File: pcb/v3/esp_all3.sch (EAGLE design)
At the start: 23 parts

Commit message: updated schematic
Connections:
- net N$25 renamed 3V3
- net N$26 renamed DHT_SIG
- net N$28 renamed TTL_DIMM
- removed net N$23: ESP.D5
- removed net N$29: ESP.D1, PIR.OUT
- new net N$16: ESP.D1
- new net PIR: ESP.D5, PIR.OUT
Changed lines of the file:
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@@
 </segment>
 </net>
-<net name="N$23" class="0">
+<net name="PIR" class="0">
 <segment>
 <pinref part="ESP" gate="G$1" pin="D5"/>
-<wire x1="93.98" y1="45.72" x2="99.06" y2="45.72" width="0.1524" layer="91"/>
-</segment>
-</net>
-<net name="N$26" class="0">
+<wire x1="93.98" y1="45.72" x2="111.76" y2="45.72" width="0.1524" layer="91"/>
+<wire x1="111.76" y1="45.72" x2="111.76" y2="83.82" width="0.1524" layer="91"/>
+<pinref part="PIR" gate="G$1" pin="OUT"/>
+<wire x1="111.76" y1="83.82" x2="-5.08" y2="83.82" width="0.1524" layer="91"/>
+<wire x1="-5.08" y1="83.82" x2="-5.08" y2="88.9" width="0.1524" layer="91"/>
+</segment>
+</net>
+<net name="DHT_SIG" class="0">
 <segment>
 <pinref part="ESP" gate="G$1" pin="D4"/>
@@
 </segment>
 </net>
-<net name="N$28" class="0">
+<net name="TTL_DIMM" class="0">
 <segment>
 <pinref part="ESP" gate="G$1" pin="D2"/>
@@
 <pinref part="DIMMING" gate="G$1" pin="G"/>
 <wire x1="132.08" y1="88.9" x2="104.14" y2="88.9" width="0.1524" layer="91"/>
-</segment>
-</net>
-<net name="N$29" class="0">
-<segment>
-<pinref part="ESP" gate="G$1" pin="D1"/>
-<wire x1="93.98" y1="60.96" x2="101.6" y2="60.96" width="0.1524" layer="91"/>
-<wire x1="101.6" y1="60.96" x2="101.6" y2="83.82" width="0.1524" layer="91"/>
-<pinref part="PIR" gate="G$1" pin="OUT"/>
-<wire x1="101.6" y1="83.82" x2="-5.08" y2="83.82" width="0.1524" layer="91"/>
-<wire x1="-5.08" y1="83.82" x2="-5.08" y2="88.9" width="0.1524" layer="91"/>
 </segment>
 </net>
@@
 </segment>
 </net>
-<net name="N$25" class="0">
+<net name="3V3" class="0">
 <segment>
 <wire x1="111.76" y1="27.94" x2="119.38" y2="27.94" width="0.1524" layer="91"/>
@@
 </segment>
 </net>
+<net name="N$16" class="0">
+<segment>
+<pinref part="ESP" gate="G$1" pin="D1"/>
+<wire x1="93.98" y1="60.96" x2="101.6" y2="60.96" width="0.1524" layer="91"/>
+</segment>
+</net>

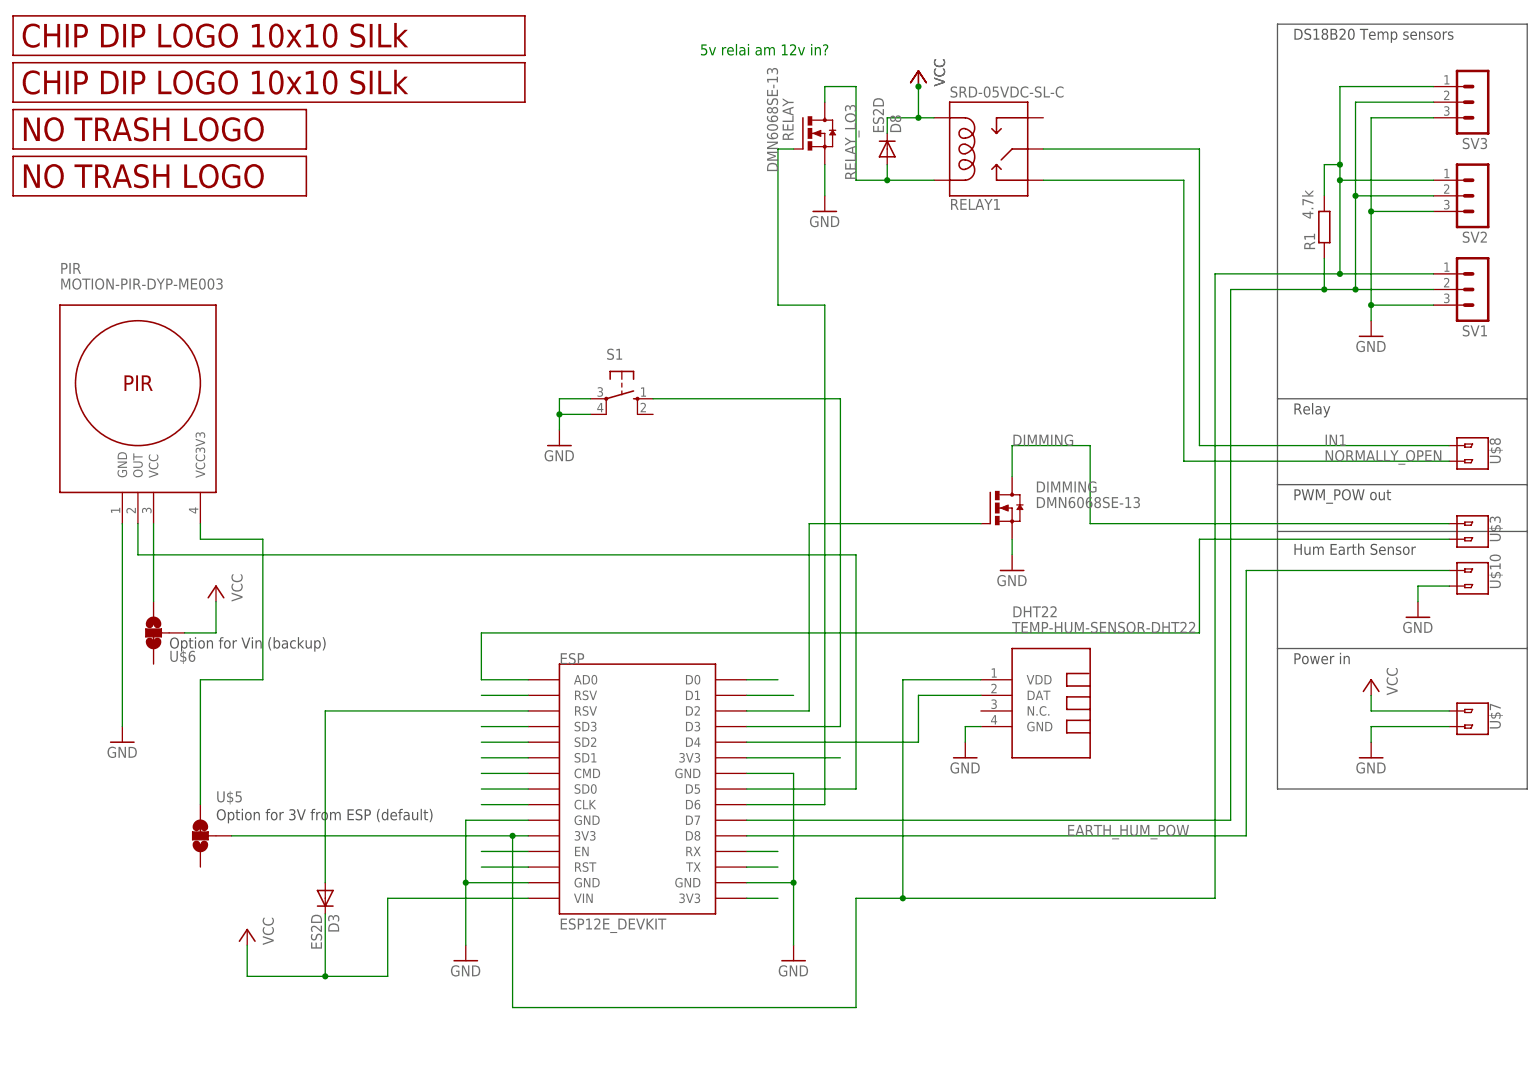
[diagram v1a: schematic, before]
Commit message: added LDO
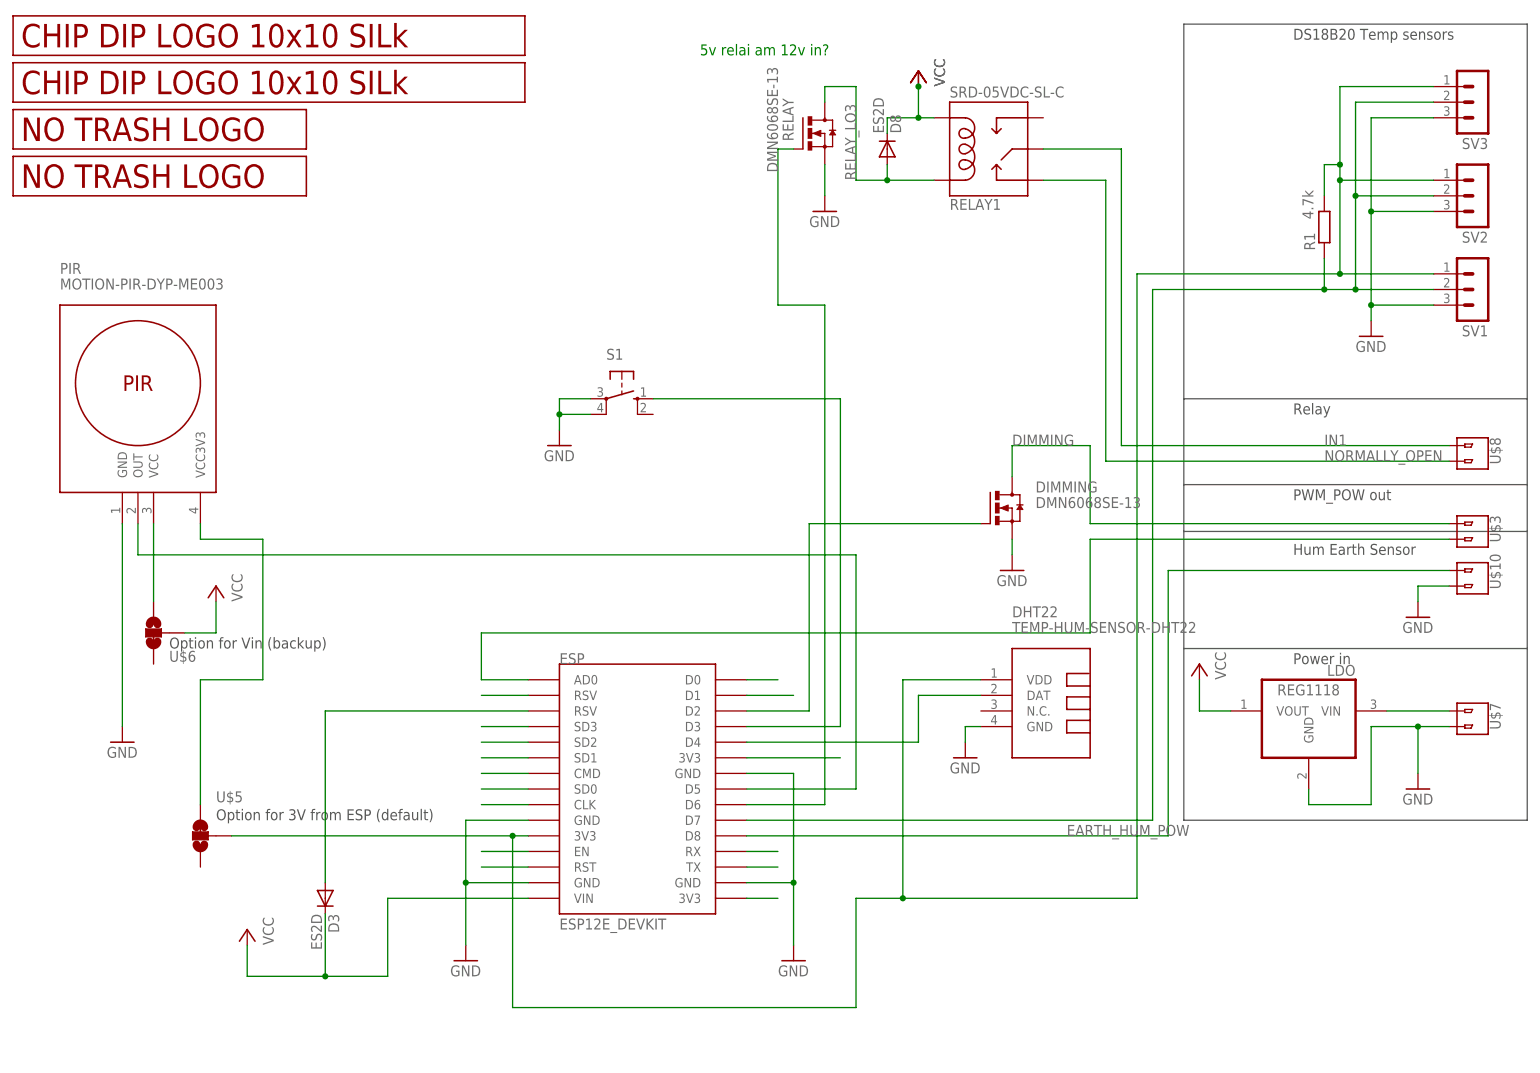
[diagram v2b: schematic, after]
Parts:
- added LDO: REG1118, burr-brown:REG1118
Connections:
- new net N$17: LDO.VIN, U$7.1
- net GND: now also LDO.GND
- net VCC: now also LDO.VOUT; no longer U$7.1
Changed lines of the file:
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@@
 <part name="U$11" library="JKW_CHIP" deviceset="LOGO_10X10_SILK" device=""/>
 <part name="D3" library="diode" deviceset="ES2D" device=""/>
+<part name="LDO" library="burr-brown" deviceset="REG1118" device=""/>
 </parts>
 <sheets>
@@
 <text x="86.36" y="165.1" size="1.778" layer="91">5v relai am 12v in? </text>
 <wire x1="220.98" y1="109.22" x2="220.98" y2="170.18" width="0.1524" layer="97"/>
-<wire x1="220.98" y1="170.18" x2="180.34" y2="170.18" width="0.1524" layer="97"/>
-<wire x1="180.34" y1="170.18" x2="180.34" y2="109.22" width="0.1524" layer="97"/>
+<wire x1="220.98" y1="170.18" x2="165.1" y2="170.18" width="0.1524" layer="97"/>
+<wire x1="165.1" y1="170.18" x2="165.1" y2="109.22" width="0.1524" layer="97"/>
 <text x="182.88" y="167.64" size="1.778" layer="97">DS18B20 Temp sensors</text>
-<wire x1="180.34" y1="109.22" x2="220.98" y2="109.22" width="0.1524" layer="97"/>
+<wire x1="165.1" y1="109.22" x2="220.98" y2="109.22" width="0.1524" layer="97"/>
 <wire x1="220.98" y1="109.22" x2="220.98" y2="95.25" width="0.1524" layer="97"/>
-<wire x1="180.34" y1="95.25" x2="180.34" y2="109.22" width="0.1524" layer="97"/>
+<wire x1="165.1" y1="95.25" x2="165.1" y2="109.22" width="0.1524" layer="97"/>
 <text x="182.88" y="106.68" size="1.778" layer="97">Relay</text>
-<wire x1="180.34" y1="87.63" x2="220.98" y2="87.63" width="0.1524" layer="97"/>
+<wire x1="165.1" y1="87.63" x2="220.98" y2="87.63" width="0.1524" layer="97"/>
 <wire x1="220.98" y1="87.63" x2="220.98" y2="95.25" width="0.1524" layer="97"/>
-<wire x1="220.98" y1="95.25" x2="180.34" y2="95.25" width="0.1524" layer="97"/>
-<wire x1="180.34" y1="95.25" x2="180.34" y2="87.63" width="0.1524" layer="97"/>
-<wire x1="180.34" y1="87.63" x2="180.34" y2="68.58" width="0.1524" layer="97"/>
+<wire x1="220.98" y1="95.25" x2="165.1" y2="95.25" width="0.1524" layer="97"/>
+<wire x1="165.1" y1="95.25" x2="165.1" y2="87.63" width="0.1524" layer="97"/>
+<wire x1="165.1" y1="87.63" x2="165.1" y2="68.58" width="0.1524" layer="97"/>
 <wire x1="220.98" y1="68.58" x2="220.98" y2="87.63" width="0.1524" layer="97"/>
 <text x="182.88" y="92.71" size="1.778" layer="97">PWM_POW out</text>
 <text x="182.88" y="83.82" size="1.778" layer="97">Hum Earth Sensor</text>
-<wire x1="180.34" y1="68.58" x2="220.98" y2="68.58" width="0.1524" layer="97"/>
-<wire x1="220.98" y1="68.58" x2="220.98" y2="45.72" width="0.1524" layer="97"/>
-<wire x1="220.98" y1="45.72" x2="180.34" y2="45.72" width="0.1524" layer="97"/>
-<wire x1="180.34" y1="45.72" x2="180.34" y2="68.58" width="0.1524" layer="97"/>
+<wire x1="165.1" y1="68.58" x2="220.98" y2="68.58" width="0.1524" layer="97"/>
+<wire x1="220.98" y1="68.58" x2="220.98" y2="40.64" width="0.1524" layer="97"/>
+<wire x1="220.98" y1="40.64" x2="165.1" y2="40.64" width="0.1524" layer="97"/>
+<wire x1="165.1" y1="40.64" x2="165.1" y2="68.58" width="0.1524" layer="97"/>
 <text x="182.88" y="66.04" size="1.778" layer="97">Power in</text>
 <text x="7.62" y="40.64" size="1.778" layer="97">Option for 3V from ESP (default)</text>
@@
 <attribute name="NAME" x="216.662" y="55.372" size="1.778" layer="95" rot="R90"/>
 </instance>
-<instance part="P+1" gate="VCC" x="195.58" y="63.5" rot="MR0"/>
-<instance part="GND4" gate="1" x="195.58" y="50.8"/>
+<instance part="P+1" gate="VCC" x="167.64" y="66.04" rot="MR0"/>
+<instance part="GND4" gate="1" x="203.2" y="45.72"/>
 <instance part="P+2" gate="VCC" x="12.7" y="22.86" rot="MR0"/>
 <instance part="P+3" gate="VCC" x="7.62" y="78.74" rot="MR0"/>
@@
 <instance part="U$11" gate="G$1" x="-25.4" y="157.48"/>
 <instance part="D3" gate="G$1" x="25.4" y="27.94" rot="R270"/>
+<instance part="LDO" gate="G$1" x="185.42" y="58.42" rot="MR0"/>
 </instances>
 <busses>
@@
 <wire x1="58.42" y1="63.5" x2="50.8" y2="63.5" width="0.1524" layer="91"/>
 <wire x1="50.8" y1="63.5" x2="50.8" y2="71.12" width="0.1524" layer="91"/>
-<wire x1="50.8" y1="71.12" x2="167.64" y2="71.12" width="0.1524" layer="91"/>
+<wire x1="50.8" y1="71.12" x2="149.86" y2="71.12" width="0.1524" layer="91"/>
 <pinref part="U$3" gate="G$1" pin="2"/>
-<wire x1="208.28" y1="86.36" x2="167.64" y2="86.36" width="0.1524" layer="91"/>
-<wire x1="167.64" y1="86.36" x2="167.64" y2="71.12" width="0.1524" layer="91"/>
+<wire x1="208.28" y1="86.36" x2="149.86" y2="86.36" width="0.1524" layer="91"/>
+<wire x1="149.86" y1="86.36" x2="149.86" y2="71.12" width="0.1524" layer="91"/>
 </segment>
 </net>
@@
 <segment>
 <pinref part="ESP" gate="G$1" pin="D8"/>
-<wire x1="93.98" y1="38.1" x2="175.26" y2="38.1" width="0.1524" layer="91"/>
-<wire x1="175.26" y1="38.1" x2="175.26" y2="81.28" width="0.1524" layer="91"/>
+<wire x1="93.98" y1="38.1" x2="162.56" y2="38.1" width="0.1524" layer="91"/>
+<wire x1="162.56" y1="38.1" x2="162.56" y2="81.28" width="0.1524" layer="91"/>
 <pinref part="U$10" gate="G$1" pin="1"/>
-<wire x1="208.28" y1="81.28" x2="175.26" y2="81.28" width="0.1524" layer="91"/>
+<wire x1="208.28" y1="81.28" x2="162.56" y2="81.28" width="0.1524" layer="91"/>
 <label x="146.05" y="38.1" size="1.778" layer="95"/>
 </segment>
@@
 <pinref part="U$7" gate="G$1" pin="2"/>
 <pinref part="GND4" gate="1" pin="GND"/>
-<wire x1="208.28" y1="55.88" x2="195.58" y2="55.88" width="0.1524" layer="91"/>
-<wire x1="195.58" y1="55.88" x2="195.58" y2="53.34" width="0.1524" layer="91"/>
+<wire x1="208.28" y1="55.88" x2="203.2" y2="55.88" width="0.1524" layer="91"/>
+<wire x1="203.2" y1="55.88" x2="203.2" y2="48.26" width="0.1524" layer="91"/>
+<pinref part="LDO" gate="G$1" pin="GND"/>
+<wire x1="185.42" y1="45.72" x2="185.42" y2="43.18" width="0.1524" layer="91"/>
+<wire x1="185.42" y1="43.18" x2="195.58" y2="43.18" width="0.1524" layer="91"/>
+<wire x1="195.58" y1="43.18" x2="195.58" y2="55.88" width="0.1524" layer="91"/>
+<wire x1="195.58" y1="55.88" x2="203.2" y2="55.88" width="0.1524" layer="91"/>
+<junction x="203.2" y="55.88"/>
 </segment>
 <segment>
@@
 </segment>
 <segment>
-<pinref part="U$7" gate="G$1" pin="1"/>
 <pinref part="P+1" gate="VCC" pin="VCC"/>
-<wire x1="208.28" y1="58.42" x2="195.58" y2="58.42" width="0.1524" layer="91"/>
-<wire x1="195.58" y1="58.42" x2="195.58" y2="60.96" width="0.1524" layer="91"/>
+<pinref part="LDO" gate="G$1" pin="VOUT"/>
+<wire x1="172.72" y1="58.42" x2="167.64" y2="58.42" width="0.1524" layer="91"/>
+<wire x1="167.64" y1="58.42" x2="167.64" y2="63.5" width="0.1524" layer="91"/>
 </segment>
 <segment>
@@
 <segment>
 <pinref part="RELAY1" gate="G$1" pin="SWCLOSE"/>
-<wire x1="165.1" y1="144.78" x2="142.24" y2="144.78" width="0.1524" layer="91"/>
-<wire x1="165.1" y1="144.78" x2="165.1" y2="99.06" width="0.1524" layer="91"/>
+<wire x1="152.4" y1="144.78" x2="142.24" y2="144.78" width="0.1524" layer="91"/>
+<wire x1="152.4" y1="144.78" x2="152.4" y2="99.06" width="0.1524" layer="91"/>
 <label x="187.96" y="99.06" size="1.778" layer="95"/>
 <pinref part="U$8" gate="G$1" pin="2"/>
-<wire x1="208.28" y1="99.06" x2="165.1" y2="99.06" width="0.1524" layer="91"/>
+<wire x1="208.28" y1="99.06" x2="152.4" y2="99.06" width="0.1524" layer="91"/>
 </segment>
 </net>
@@
 <segment>
 <pinref part="RELAY1" gate="G$1" pin="SWCOMMON"/>
-<wire x1="142.24" y1="149.86" x2="167.64" y2="149.86" width="0.1524" layer="91"/>
-<wire x1="167.64" y1="149.86" x2="167.64" y2="101.6" width="0.1524" layer="91"/>
+<wire x1="142.24" y1="149.86" x2="154.94" y2="149.86" width="0.1524" layer="91"/>
+<wire x1="154.94" y1="149.86" x2="154.94" y2="101.6" width="0.1524" layer="91"/>
 <pinref part="U$8" gate="G$1" pin="1"/>
-<wire x1="208.28" y1="101.6" x2="167.64" y2="101.6" width="0.1524" layer="91"/>
+<wire x1="208.28" y1="101.6" x2="154.94" y2="101.6" width="0.1524" layer="91"/>
 <label x="187.96" y="101.6" size="1.778" layer="95"/>
 </segment>
@@
 <net name="N$15" class="0">
 <segment>
-<wire x1="172.72" y1="40.64" x2="172.72" y2="127" width="0.1524" layer="91"/>
-<wire x1="172.72" y1="127" x2="187.96" y2="127" width="0.1524" layer="91"/>
+<wire x1="160.02" y1="40.64" x2="160.02" y2="127" width="0.1524" layer="91"/>
+<wire x1="160.02" y1="127" x2="187.96" y2="127" width="0.1524" layer="91"/>
 <pinref part="R1" gate="G$1" pin="1"/>
 <wire x1="187.96" y1="132.08" x2="187.96" y2="127" width="0.1524" layer="91"/>
@@
 <junction x="187.96" y="127"/>
 <pinref part="ESP" gate="G$1" pin="D7"/>
-<wire x1="172.72" y1="40.64" x2="93.98" y2="40.64" width="0.1524" layer="91"/>
+<wire x1="160.02" y1="40.64" x2="93.98" y2="40.64" width="0.1524" layer="91"/>
 </segment>
 </net>
@@
 <segment>
 <wire x1="111.76" y1="27.94" x2="119.38" y2="27.94" width="0.1524" layer="91"/>
-<wire x1="119.38" y1="27.94" x2="170.18" y2="27.94" width="0.1524" layer="91"/>
-<wire x1="170.18" y1="27.94" x2="170.18" y2="129.54" width="0.1524" layer="91"/>
-<wire x1="170.18" y1="129.54" x2="190.5" y2="129.54" width="0.1524" layer="91"/>
+<wire x1="119.38" y1="27.94" x2="157.48" y2="27.94" width="0.1524" layer="91"/>
+<wire x1="157.48" y1="27.94" x2="157.48" y2="129.54" width="0.1524" layer="91"/>
+<wire x1="157.48" y1="129.54" x2="190.5" y2="129.54" width="0.1524" layer="91"/>
 <pinref part="SV3" gate="G$1" pin="1"/>
 <wire x1="190.5" y1="129.54" x2="190.5" y2="144.78" width="0.1524" layer="91"/>
@@
 </segment>
 </net>
+<net name="N$17" class="0">
+<segment>
+<pinref part="U$7" gate="G$1" pin="1"/>
+<wire x1="208.28" y1="58.42" x2="198.12" y2="58.42" width="0.1524" layer="91"/>
+<pinref part="LDO" gate="G$1" pin="VIN"/>
+</segment>
+</net>

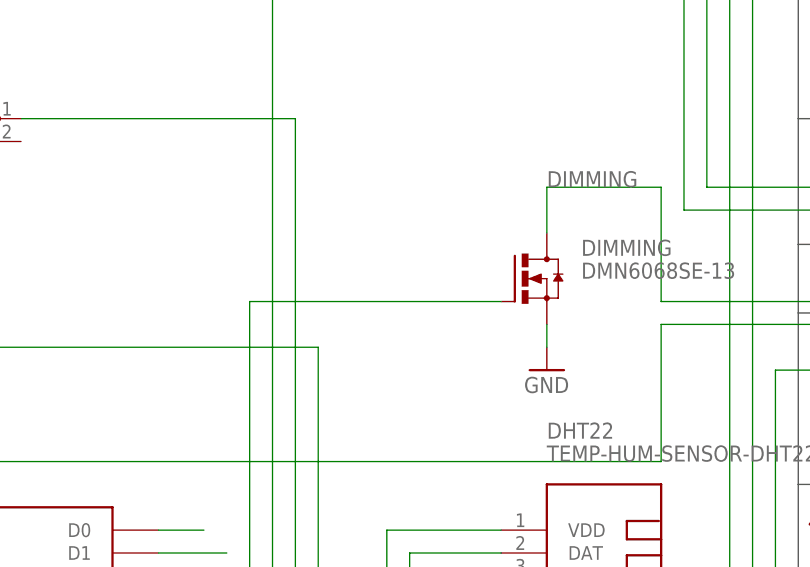
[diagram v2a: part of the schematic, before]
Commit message: added double footprint for power transistor
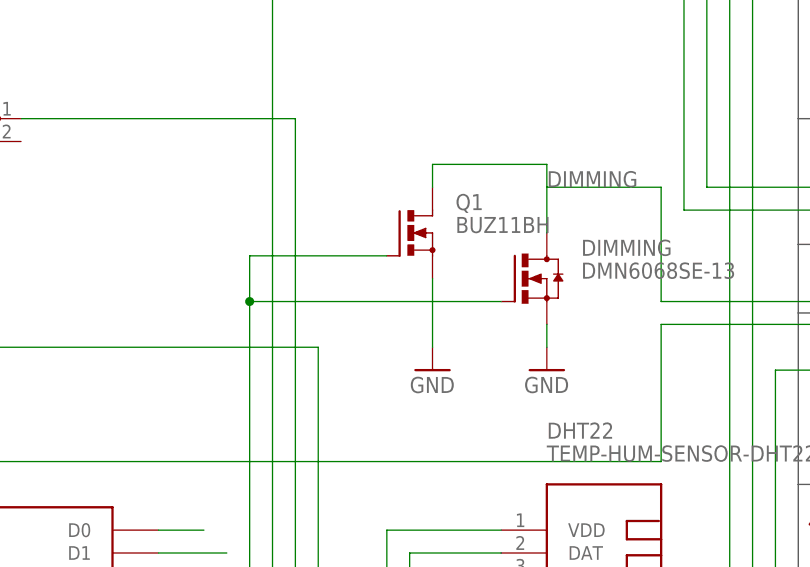
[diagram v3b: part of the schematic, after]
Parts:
- added Q1: BUZ11BH, transistor-power:BUZ11BH
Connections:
- net DIMMING: now also Q1.D
- net GND: now also Q1.S
- net TTL_DIMM: now also Q1.G
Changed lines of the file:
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@@
 <part name="D3" library="diode" deviceset="ES2D" device=""/>
 <part name="LDO" library="burr-brown" deviceset="REG1118" device=""/>
+<part name="Q1" library="transistor-power" deviceset="BUZ11" device="BH"/>
+<part name="GND11" library="supply1" deviceset="GND" device=""/>
 </parts>
 <sheets>
@@
 <instance part="D3" gate="G$1" x="25.4" y="27.94" rot="R270"/>
 <instance part="LDO" gate="G$1" x="185.42" y="58.42" rot="MR0"/>
+<instance part="Q1" gate="1" x="121.92" y="96.52"/>
+<instance part="GND11" gate="1" x="124.46" y="81.28"/>
 </instances>
 <busses>
@@
 <pinref part="DIMMING" gate="G$1" pin="G"/>
 <wire x1="132.08" y1="88.9" x2="104.14" y2="88.9" width="0.1524" layer="91"/>
+<pinref part="Q1" gate="1" pin="G"/>
+<wire x1="119.38" y1="93.98" x2="104.14" y2="93.98" width="0.1524" layer="91"/>
+<wire x1="104.14" y1="93.98" x2="104.14" y2="88.9" width="0.1524" layer="91"/>
+<junction x="104.14" y="88.9"/>
 </segment>
 </net>
@@
 <junction x="63.5" y="106.68"/>
 </segment>
+<segment>
+<pinref part="Q1" gate="1" pin="S"/>
+<pinref part="GND11" gate="1" pin="GND"/>
+<wire x1="124.46" y1="91.44" x2="124.46" y2="83.82" width="0.1524" layer="91"/>
+</segment>
 </net>
 <net name="VCC" class="0">
@@
 <wire x1="149.86" y1="88.9" x2="208.28" y2="88.9" width="0.1524" layer="91"/>
 <label x="137.16" y="101.6" size="1.778" layer="95"/>
-</segment>
-</net>
+<wire x1="137.16" y1="101.6" x2="137.16" y2="104.14" width="0.1524" layer="91"/>
+<wire x1="137.16" y1="104.14" x2="124.46" y2="104.14" width="0.1524" layer="91"/>
+<pinref part="Q1" gate="1" pin="D"/>
+<wire x1="124.46" y1="104.14" x2="124.46" y2="101.6" width="0.1524" layer="91"/>
+</segment>
+</net>
